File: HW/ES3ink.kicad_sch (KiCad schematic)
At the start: 68 parts, among them J1 USB_C_Receptacle_USB2.0, J2 Conn_01x24_Pin, J2 USB_C_Receptacle_USB2.0, J3 Conn_01x02_Pin, J4 Conn_01x04_Socket, Q1 AO3401A, Q2 SI1308EDL-T1-GE3, Q3 DMP2045U-7, Q4 SI2305, SW1 RESET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

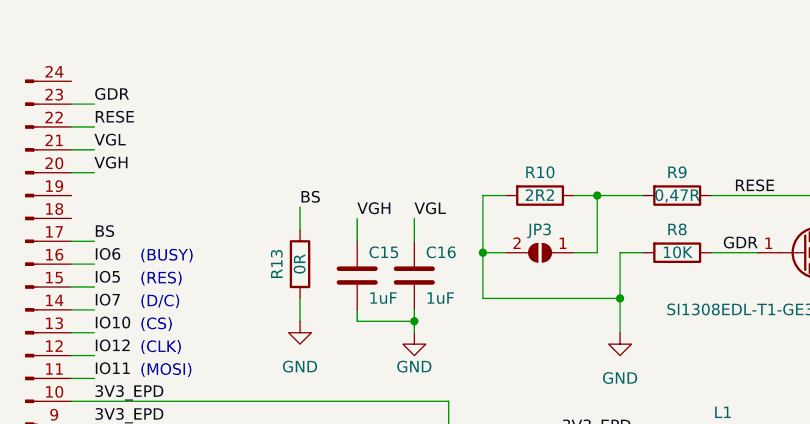
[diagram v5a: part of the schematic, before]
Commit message: Update
- component value change
- FPC connector changed to double side connection
- version increase to 1.1
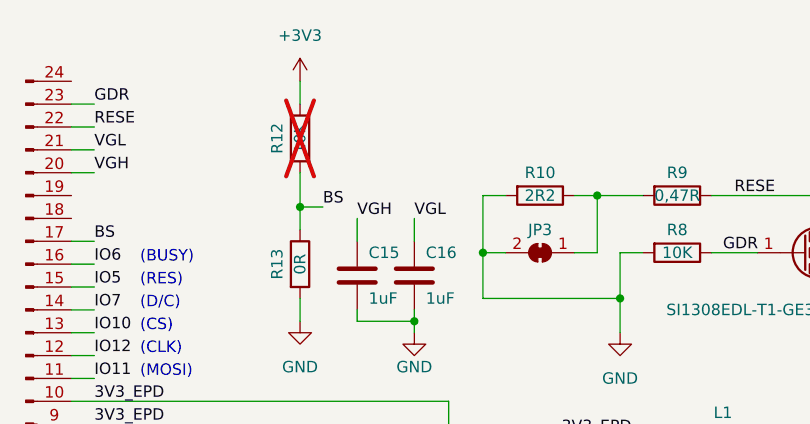
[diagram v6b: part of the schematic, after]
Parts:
- added R12: 10K, Resistor_SMD:R_0805_2012Metric, symbol Device:R
- D1, D2, D3: value MBR0520LT -> MBR0530
- J2: footprint Connector_FFC-FPC:TE_2-1734839-4_1x24-1MP_P0.5mm_Horizontal -> dronecz:GCT_FFC2B28-24-G
- JP3: footprint Jumper:SolderJumper-2_P1.3mm_Open_TrianglePad1.0x1.5mm -> Jumper:SolderJumper-2_P1.3mm_Bridged_RoundedPad1.0x1.5mm; symbol Jumper:SolderJumper_2_Open -> Jumper:SolderJumper_2_Bridged
- L1: Mouser (none) -> LQH43PN100M26L
- Q2: footprint Package_TO_SOT_SMD:SOT-23 -> Package_TO_SOT_SMD:SOT-323_SC-70
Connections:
- net +3V3: now also R12.1
- net BS: now also R12.2
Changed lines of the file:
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@@
   (junction (at 168.91 91.44) (diameter 0) (color 0 0 0 0)
   )
+  (junction (at 181.61 34.29) (diameter 0) (color 0 0 0 0)
+  )
   (junction (at 141.605 84.455) (diameter 0) (color 0 0 0 0)
   )
@@
     (stroke (width 0) (type default))
   )
+  (wire (pts (xy 181.61 34.29) (xy 184.15 34.29))
+    (stroke (width 0) (type default))
+  )
   (wire (pts (xy 137.16 147.32) (xy 139.7 147.32))
     (stroke (width 0) (type default))
@@
     (stroke (width 0) (type default))
   )
+  (wire (pts (xy 181.61 30.48) (xy 181.61 34.29))
+    (stroke (width 0) (type default))
+  )
   (wire (pts (xy 95.25 180.34) (xy 99.06 180.34))
     (stroke (width 0) (type default))
@@
     (stroke (width 0) (type default))
   )
+  (wire (pts (xy 181.61 20.32) (xy 181.61 22.86))
+    (stroke (width 0) (type default))
+  )
   (wire (pts (xy 194.31 153.67) (xy 194.31 154.94))
     (stroke (width 0) (type default))
@@
     (effects (font (size 1.27 1.27)) (justify left bottom))
   )
-  (label "BS" (at 181.61 34.29 0) (fields_autoplaced)
+  (label "BS" (at 184.15 34.29 0) (fields_autoplaced)
     (effects (font (size 1.27 1.27)) (justify left bottom))
   )
@@
       (effects (font (size 1.27 1.27)))
     )
-    (property "Value" "MBR0520LT" (at 232.41 78.74 0)
+    (property "Value" "MBR0530" (at 232.41 78.74 0)
       (effects (font (size 1.27 1.27)) hide)
     )
@@
       (effects (font (size 1.27 1.27)) (justify right))
     )
-    (property "Value" "MBR0520LT" (at 226.06 80.9625 90)
+    (property "Value" "MBR0530" (at 226.06 80.9625 90)
       (effects (font (size 1.27 1.27)) (justify right) hide)
     )
@@
       (effects (font (size 1.27 1.27)) (justify right))
     )
-    (property "Footprint" "Package_TO_SOT_SMD:SOT-23" (at 242.57 37.465 0)
+    (property "Footprint" "Package_TO_SOT_SMD:SOT-323_SC-70" (at 242.57 37.465 0)
       (effects (font (size 1.27 1.27) italic) (justify left) hide)
     )
@@
     )
   )
-  (symbol (lib_id "Jumper:SolderJumper_2_Open") (at 208.28 39.37 180) (unit 1)
+  (symbol (lib_id "Jumper:SolderJumper_2_Bridged") (at 208.28 39.37 180) (unit 1)
     (in_bom yes) (on_board yes) (dnp no)
     (property "Reference" "JP3" (at 208.28 36.83 0)
@@
       (effects (font (size 1.27 1.27)) (justify right) hide)
     )
-    (property "Footprint" "Jumper:SolderJumper-2_P1.3mm_Open_TrianglePad1.0x1.5mm" (at 208.28 39.37 0)
+    (property "Footprint" "Jumper:SolderJumper-2_P1.3mm_Bridged_RoundedPad1.0x1.5mm" (at 208.28 39.37 0)
       (effects (font (size 1.27 1.27)) hide)
     )
@@
     )
   )
+  (symbol (lib_id "power:+3V3") (at 181.61 20.32 0) (unit 1)
+    (in_bom yes) (on_board yes) (dnp no) (fields_autoplaced)
+    (property "Reference" "#PWR029" (at 181.61 24.13 0)
+      (effects (font (size 1.27 1.27)) hide)
+    )
+    (property "Value" "+3V3" (at 181.61 15.24 0)
+      (effects (font (size 1.27 1.27)))
+    )
+    (property "Footprint" "" (at 181.61 20.32 0)
+      (effects (font (size 1.27 1.27)) hide)
+    )
+    (property "Datasheet" "" (at 181.61 20.32 0)
+      (effects (font (size 1.27 1.27)) hide)
+    )
+    (pin "1")
+    (instances
+      (project "ES3ink"
+        (path "/571f6350-75eb-4507-91d1-3317b5ffe0b6"
+          (reference "#PWR029") (unit 1)
+        )
+      )
+      (project "LazyMiniGrid_S3_mini_rev_Bi2"
+        (path "/c1eb7fdd-5d4c-4207-ae81-c19f49c51f35"
+          (reference "#PWR014") (unit 1)
+        )
+      )
+    )
+  )
   (symbol (lib_id "power:+5V") (at 64.77 162.56 0) (unit 1)
     (in_bom yes) (on_board yes) (dnp no)
@@
     )
   )
+  (symbol (lib_id "Device:R") (at 181.61 26.67 0) (unit 1)
+    (in_bom yes) (on_board yes) (dnp yes)
+    (property "Reference" "R12" (at 179.07 26.67 90)
+      (effects (font (size 1.27 1.27)))
+    )
+    (property "Value" "10K" (at 181.61 26.67 90)
+      (effects (font (size 1.27 1.27)))
+    )
+    (property "Footprint" "Resistor_SMD:R_0805_2012Metric" (at 179.832 26.67 90)
+      (effects (font (size 1.27 1.27)) hide)
+    )
+    (property "Datasheet" "~" (at 181.61 26.67 0)
+      (effects (font (size 1.27 1.27)) hide)
+    )
+    (pin "1")
+    (pin "2")
+    (instances
+      (project "ES3ink"
+        (path "/571f6350-75eb-4507-91d1-3317b5ffe0b6"
+          (reference "R12") (unit 1)
+        )
+      )
+      (project "LazyMiniGrid_S3_mini_rev_Bi2"
+        (path "/c1eb7fdd-5d4c-4207-ae81-c19f49c51f35"
+          (reference "R6") (unit 1)
+        )
+      )
+    )
+  )
   (symbol (lib_id "power:+5V") (at 31.75 147.32 0) (unit 1)
     (in_bom yes) (on_board yes) (dnp no)
@@
       (effects (font (size 1.27 1.27)) hide)
     )
+    (property "Mouser" "LQH43PN100M26L" (at 228.6 59.69 90)
+      (effects (font (size 1.27 1.27)) hide)
+    )
     (pin "1")
     (pin "2")
@@
       (effects (font (size 1.27 1.27)))
     )
-    (property "Value" "MBR0520LT" (at 242.57 78.74 0)
+    (property "Value" "MBR0530" (at 242.57 78.74 0)
       (effects (font (size 1.27 1.27)) hide)
     )
@@
       (effects (font (size 1.27 1.27)) hide)
     )
-    (property "Footprint" "Connector_FFC-FPC:TE_2-1734839-4_1x24-1MP_P0.5mm_Horizontal" (at 151.13 50.8 0)
+    (property "Footprint" "dronecz:GCT_FFC2B28-24-G" (at 151.13 50.8 0)
       (effects (font (size 1.27 1.27)) hide)
     )

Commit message: Add title in schematic
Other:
- title: (none) -> ES3ink
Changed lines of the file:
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@@
 (kicad_sch (version 20230121) (generator eeschema)
   (paper "A4")
+  (title_block
+    (title "ES3ink")
+    (rev "P1.1")
+  )
   (junction (at 129.54 137.16) (diameter 0) (color 0 0 0 0)
   )

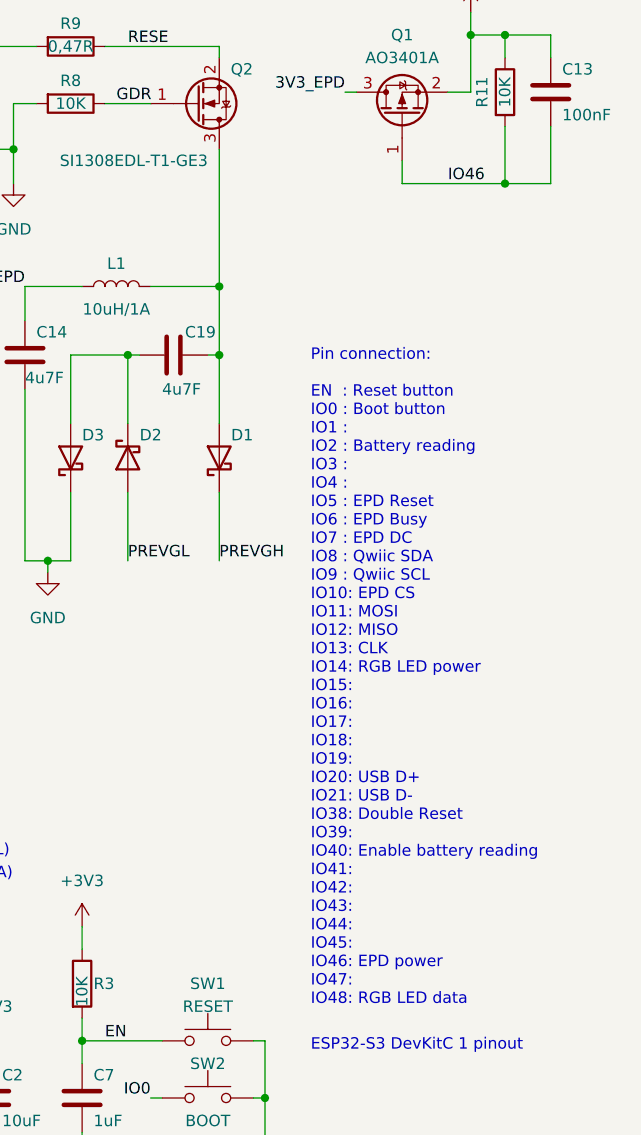
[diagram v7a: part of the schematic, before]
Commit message: Update to P1.2
- changed e-ink pwr pin to IO3
- unified reference text values
- add link to view design in KiCanvas
- version increment to P1.2
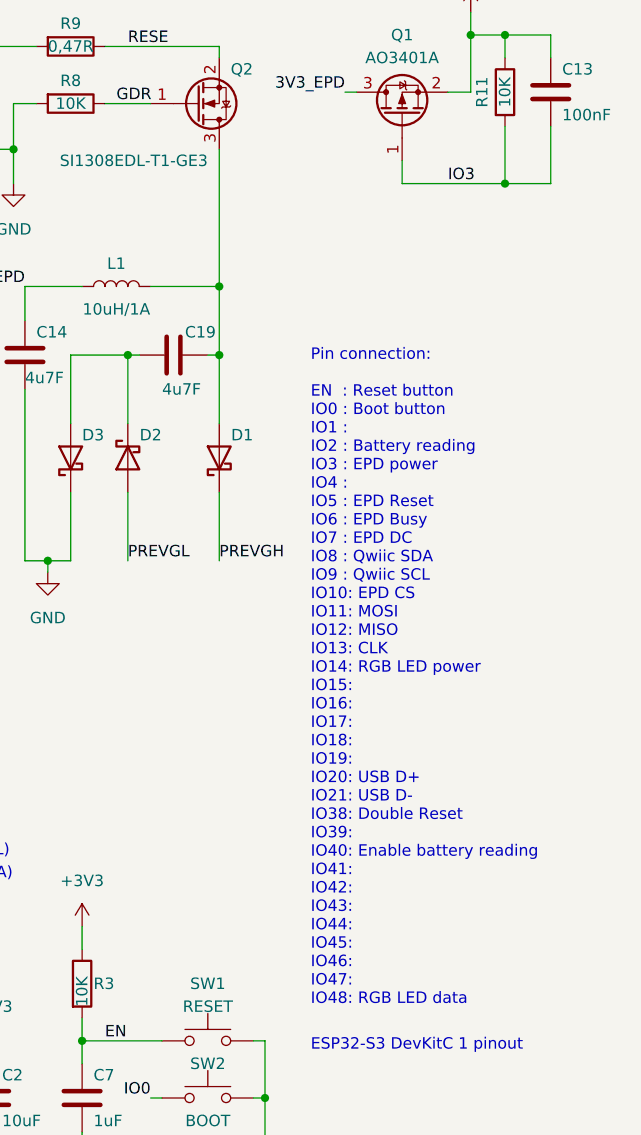
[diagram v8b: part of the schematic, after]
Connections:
- net IO3: now also C13.2, Q1.1 (G), R11.2
- net IO46: no longer C13.2, Q1.1 (G), R11.2
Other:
- note added: "Pin connection: EN : Reset button IO0 : Boot button IO1 : IO2 : Battery reading IO3 : EPD power IO4 : IO5 : EPD Reset IO6 : EPD Busy IO7 : EPD DC IO8 : Qwiic SDA IO9 : Qwiic SCL IO10: EPD CS IO11: MOSI IO12: MISO IO13: CLK IO14: RGB LED power IO15: IO16: IO17: IO18: IO19: IO20: USB D+ IO21: USB D- IO38: Double Reset IO39: IO40: Enable battery reading IO41: IO42: IO43: IO44: IO45: IO46: IO47: IO48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"
- note removed: "Pin connection: EN : Reset button IO0 : Boot button IO1 : IO2 : Battery reading IO3 : IO4 : IO5 : EPD Reset IO6 : EPD Busy IO7 : EPD DC IO8 : Qwiic SDA IO9 : Qwiic SCL IO10: EPD CS IO11: MOSI IO12: MISO IO13: CLK IO14: RGB LED power IO15: IO16: IO17: IO18: IO19: IO20: USB D+ IO21: USB D- IO38: Double Reset IO39: IO40: Enable battery reading IO41: IO42: IO43: IO44: IO45: IO46: EPD power IO47: IO48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"
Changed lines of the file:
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@@
   (title_block
     (title "ES3ink")
-    (rev "P1.1")
+    (rev "P1.2")
   )
   (junction (at 129.54 137.16) (diameter 0) (color 0 0 0 0)
@@
     (effects (font (size 1.27 1.27)) (justify left bottom))
   )
-  (text "Pin connection: \n\nEN  : Reset button\nIO0 : Boot button\nIO1 :\nIO2 : Battery reading\nIO3 : \nIO4 : \nIO5 : EPD Reset\nIO6 : EPD Busy \nIO7 : EPD DC\nIO8 : Qwiic SDA\nIO9 : Qwiic SCL\nIO10: EPD CS\nIO11: MOSI\nIO12: MISO\nIO13: CLK\nIO14: RGB LED power\nIO15: \nIO16: \nIO17:\nIO18: \nIO19:\nIO20: USB D+\nIO21: USB D-\nIO38: Double Reset\nIO39: \nIO40: Enable battery reading\nIO41: \nIO42: \nIO43: \nIO44:\nIO45:\nIO46: EPD power\nIO47:\nIO48: RGB LED data\n"
+  (text "Pin connection: \n\nEN  : Reset button\nIO0 : Boot button\nIO1 :\nIO2 : Battery reading\nIO3 : EPD power\nIO4 : \nIO5 : EPD Reset\nIO6 : EPD Busy \nIO7 : EPD DC\nIO8 : Qwiic SDA\nIO9 : Qwiic SCL\nIO10: EPD CS\nIO11: MOSI\nIO12: MISO\nIO13: CLK\nIO14: RGB LED power\nIO15: \nIO16: \nIO17:\nIO18: \nIO19:\nIO20: USB D+\nIO21: USB D-\nIO38: Double Reset\nIO39: \nIO40: Enable battery reading\nIO41: \nIO42: \nIO43: \nIO44:\nIO45:\nIO46: \nIO47:\nIO48: RGB LED data\n"
     (at 250.19 139.7 0)
     (effects (font (size 1.27 1.27)) (justify left bottom))
@@
     (effects (font (size 1.27 1.27)) (justify right bottom))
   )
-  (label "IO46" (at 265.43 48.26 0) (fields_autoplaced)
-    (effects (font (size 1.27 1.27)) (justify left bottom))
-  )
+  (label "IO3" (at 265.43 48.26 0) (fields_autoplaced)
+    (effects (font (size 1.27 1.27)) (justify left bottom))
+  )
